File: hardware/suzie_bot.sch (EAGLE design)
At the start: 21 parts, among them IC1 LT1529CT33, IC2 L9637DDIP-ADAPTED, Y1 1.8432, Y2 6.0

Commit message: Latest attempts.
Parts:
- removed U$12: 4CH-LEVEL-CONVERTER, randomjunk:4CH-LEVEL-CONVERTER
- removed U$6: SC16IS750IPWDIP-ADAPTER, nxp-semiconductors:SC16IS750IPWDIP-ADAPTER
- added U$2: SC16IS752IPW, nxp-semiconductors:SC16IS752IPW
- R1, R2: value 1K -> 1k; device rcl:R-US_0411/12 -> SparkFun-Passives:RESISTORPTH-1/6W
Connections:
- removed net N$15 (its old number): C3.1, U$7.XTAL2, Y2.1
- removed net N$18: R2.1, U$7.IRQ
- removed net N$26: U$5.TX, U$6.RX
- removed net N$27: U$5.RX, U$6.TX
- removed net N$28: R1.2, U$6.IRQ
- removed net N$31: U$1.D8, U$3.CH_PD
- removed net N$35: U$1.D7, U$5.ENABLE
- new net N$14: U$2.RXA, U$5.TX
- new net N$20: C4.1, U$7.XTAL1, Y2.2
- new net N$21: C3.2, U$7.XTAL2, Y2.1
- new net N$22: R1.2, U$2.IRQ
- new net N$5: U$2.RXB, U$3.TXD
- net 3V3: now also R2.1, U$2.VDD; no longer U$12.3V3, U$6.SDA/VSS, U$6.VDD
- net 5V: no longer R2.2, U$12.5V
- net GND: now also C1.2, C2.2, C3.1, C4.2, U$2.VSS; no longer C1.1, C2.1, C3.2, C4.1, U$12.GND, U$12.GND2, U$6.I2C/SPI, U$6.VSS, U$7.I2C/SPI, U$7.SDA/VSS
- net MISO: now also U$2.-/SO; no longer U$6.A1/SI
- net MOSI: now also U$2.A1/SI; no longer U$6.-/SO
- net N$1: now also C1.1, U$2.XTAL1, Y1.1; no longer U$1.TX0, U$12.HV4
- net N$16: now also R2.2, U$7.IRQ; no longer C4.2, U$7.XTAL1, Y2.2
- net N$17: now also U$2.TXA, U$5.RX; no longer C1.2, U$6.XTAL1, Y1.1
- net N$2: now also U$2.GPIO6/CDA, U$5.ENABLE; no longer U$12.LV4, U$3.TXD
- net N$3: now also C2.1, U$2.XTAL2, Y1.2; no longer U$12.LV3, U$3.RXD
- net N$33: now also U$2.AO/CS; no longer U$6.AO/CS
- net N$4: now also U$2.GPIO7/RIA, U$3.CH_PD; no longer U$1.RX1, U$12.HV3
- net N$8: now also U$2.TXB, U$3.RXD; no longer C2.2, U$6.XTAL2, Y1.2
- net SCLK: now also U$2.SCL/SCLK; no longer U$6.SCL/SCLK
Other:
- moved on the sheet: C1, C2, C3, C4, R1, R2, U$3, Y1, Y2

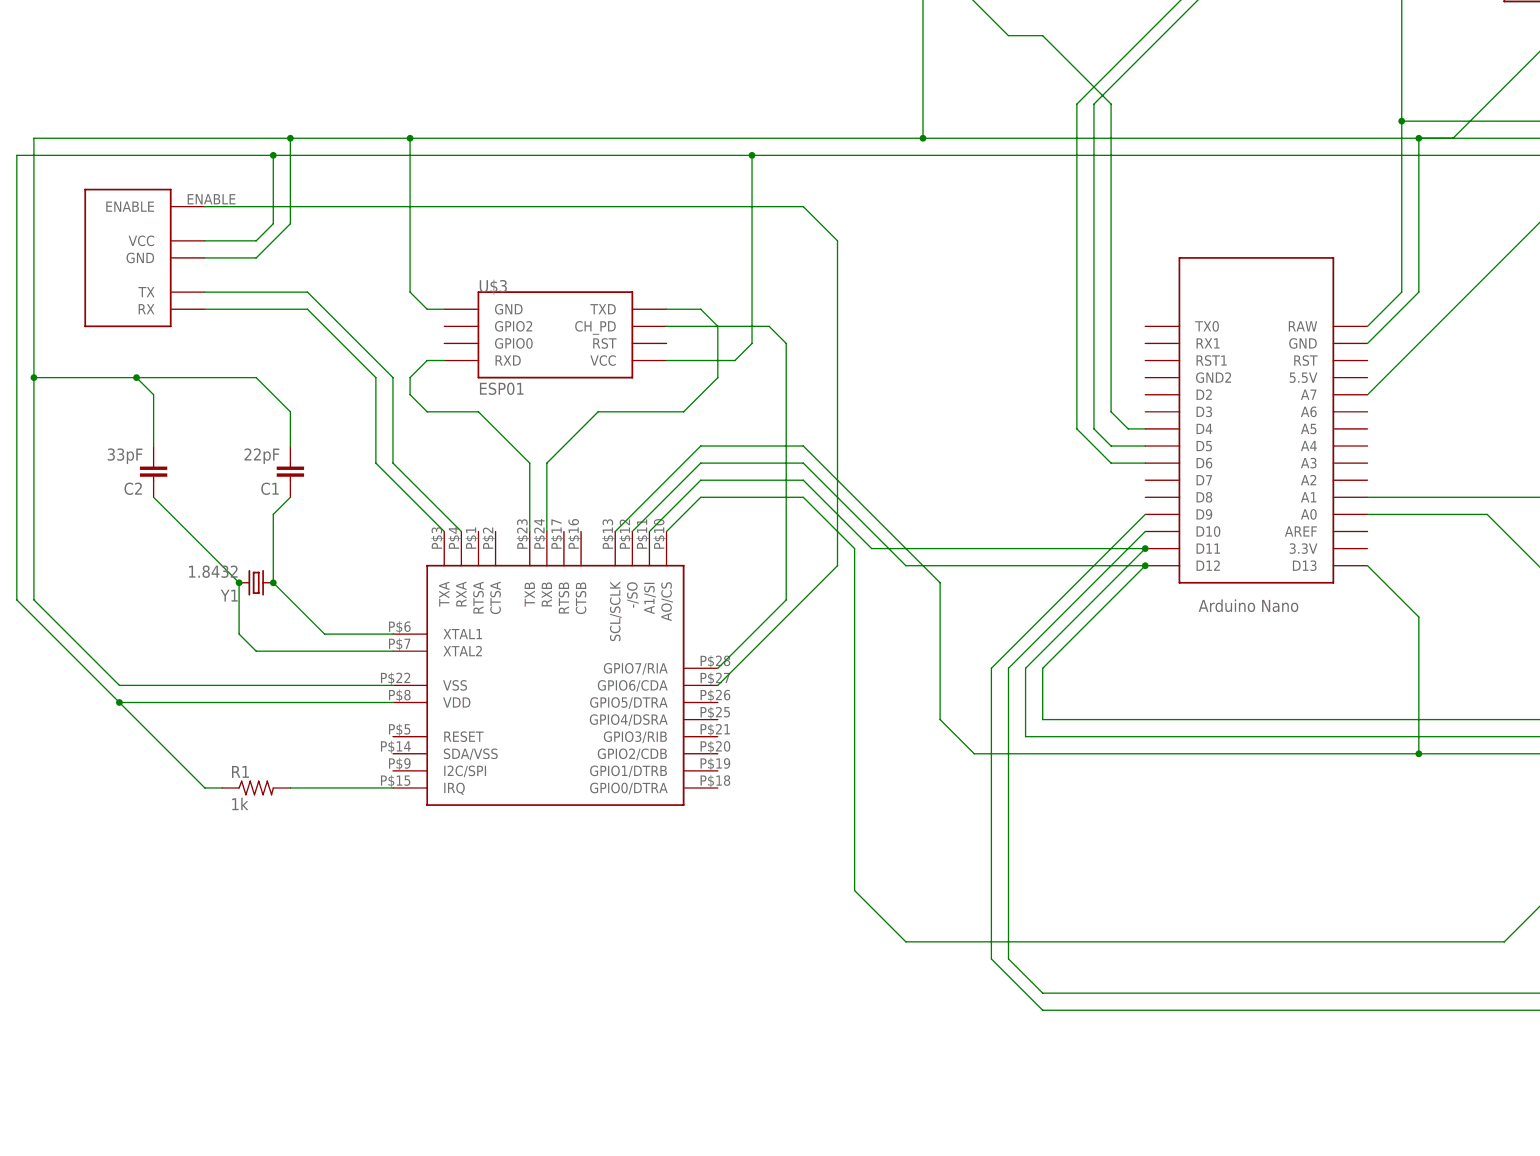
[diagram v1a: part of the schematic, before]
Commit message: Totally working. IT WAS VOLTAGE LEVELS AND CRYSTAL CAPACITANCE PROBLEMS ALL ALONG.
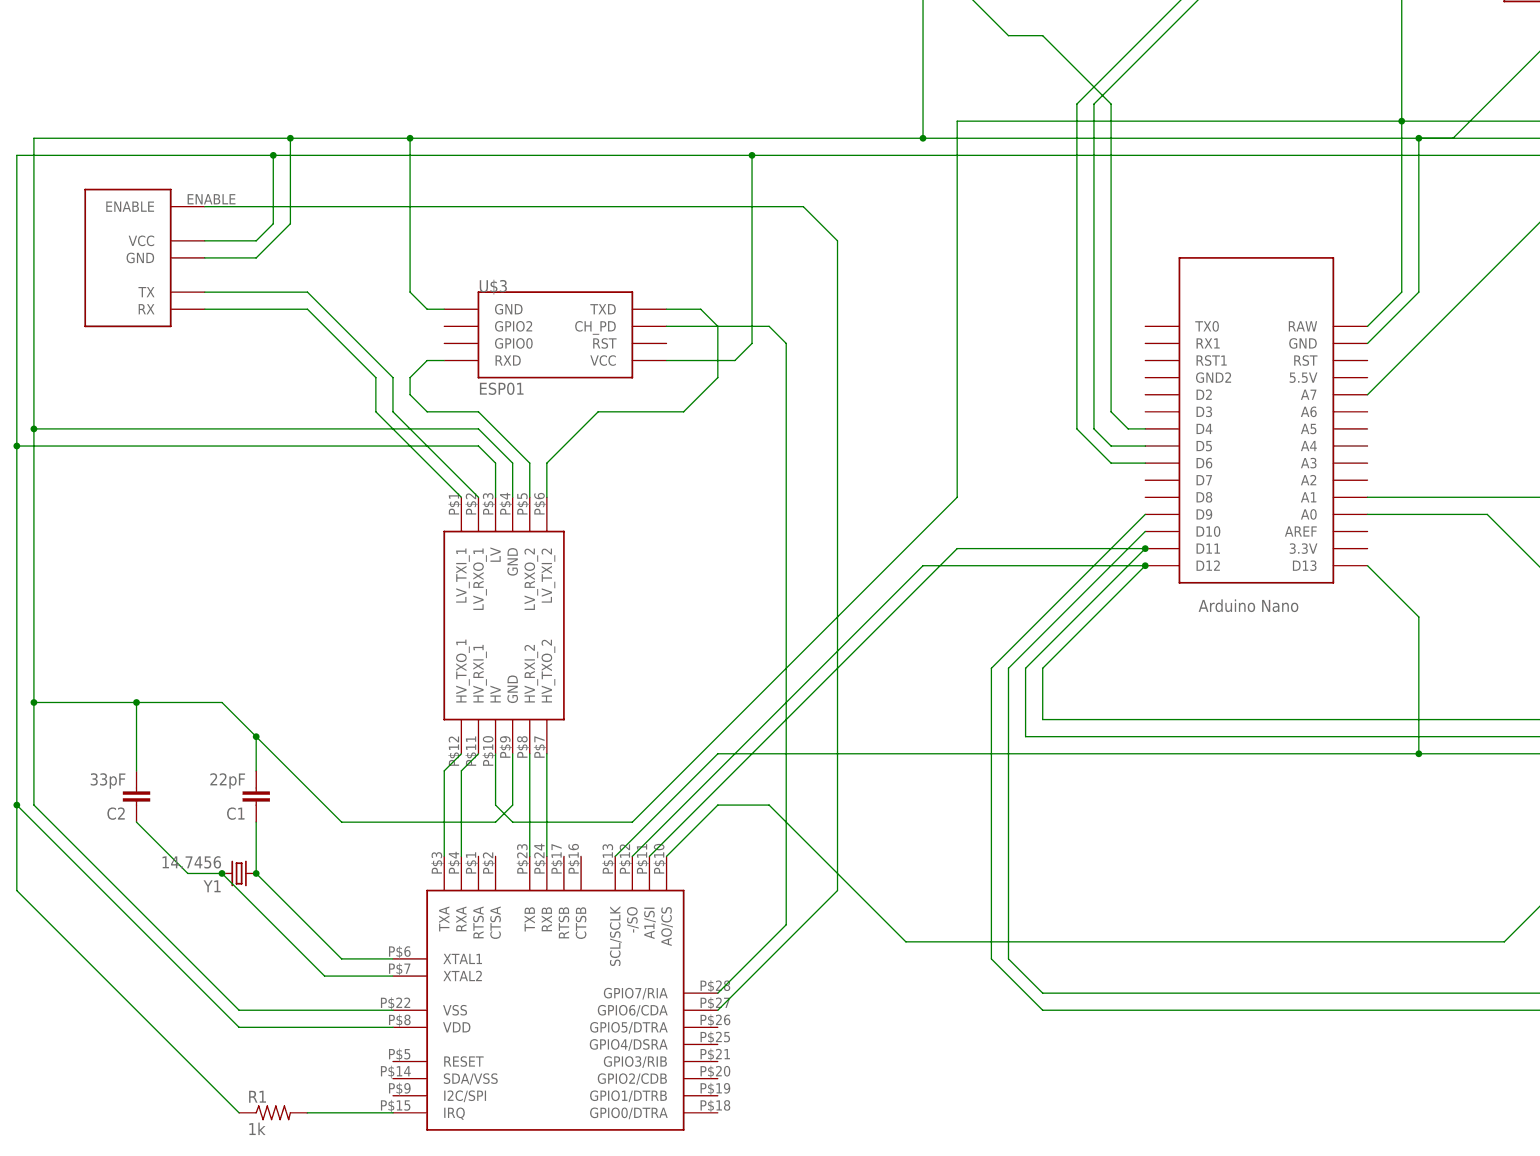
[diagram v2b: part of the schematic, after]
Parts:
- added U$6: LOGIC_LEVEL_CONVERTER, SparkFun-Boards:LOGIC_LEVEL_CONVERTER
- Y1: value 1.8432 -> 14.7456
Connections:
- new net N$22: U$2.TXB, U$6.HV_RXI_2
- new net N$23: U$2.RXB, U$6.HV_TXO_2
- new net N$24: U$2.TXA, U$6.HV_TXO_1
- new net N$25: U$2.RXA, U$6.HV_RXI_1
- net 3V3: now also U$6.LV
- net 5V: now also U$6.HV
- net GND: now also U$6.GND, U$6.GND@2
- net N$14: now also U$6.LV_RXO_1; no longer U$2.RXA
- net N$17: now also U$6.LV_TXI_1; no longer U$2.TXA
- net N$5: now also U$6.LV_TXI_2; no longer U$2.RXB
- net N$8: now also U$6.LV_RXO_2; no longer U$2.TXB
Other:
- moved on the sheet: C1, C2, R1, Y1

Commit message: Basic working features.
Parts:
- removed U$8: 9-PIN-TERMINATION-BLOCK, randomjunk:9-PIN-TERMINATION-BLOCK
- added 12V-IN/GND, 12V-OUT/ON, GND/5V, K/L: 2-PIN-TERMINAL, randomjunk:2-PIN-TERMINAL
- U$3: value ESP01 -> (none)
- U$7: value SC16IS750IPWDIP-ADAPTER -> SC16IS750IPWDIP-24; device nxp-semiconductors:SC16IS750IPWDIP-ADAPTER -> nxp-semiconductors:SC16IS750IPWDIP-24
- U$9: value LEVEL-CONVERTING-MICROSD -> (none)
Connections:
- removed net N$10: U$10.GND, U$4.GND, U$8.P$2
- removed net N$11 (its old number): U$4.ON, U$8.P$4
- removed net N$12: IC2.K, U$8.P$6
- removed net N$13: IC2.LI, U$8.P$5
- removed net N$7: IC2.VS, U$10.VCC, U$4.VIN, U$8.P$1
- removed net N$9: U$4.VOUT, U$8.P$3
- new net 12V-IN: 12V-IN/GND.P$1, U$4.VIN
- new net 12V-OUT: 12V-OUT/ON.P$1, IC2.VS, U$10.VCC, U$4.VOUT
- new net EXT-GND: 12V-IN/GND.P$2, U$10.GND, U$4.GND
- new net K: IC2.K, K/L.P$1
- new net L: IC2.LI, K/L.P$2
- new net POWERON: 12V-OUT/ON.P$2, U$4.ON
- net 5V: now also GND/5V.P$2; no longer U$8.P$8
- net GND: now also GND/5V.P$1; no longer U$8.P$9

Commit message: Adding a ground plane at @nbanerje's suggestion.  Thanks @nbanerje!
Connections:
- net 12V-IN renamed N$7
- net EXT-GND renamed EXTGND
